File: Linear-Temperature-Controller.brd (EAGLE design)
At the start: 203.2 x 34.3 mm, 78 parts, among them IC1 LM393D, IC3 AD5624R, IC4 AD5262, IC5 LF356MX, T1 MMBT3904, T2 MMBT3904

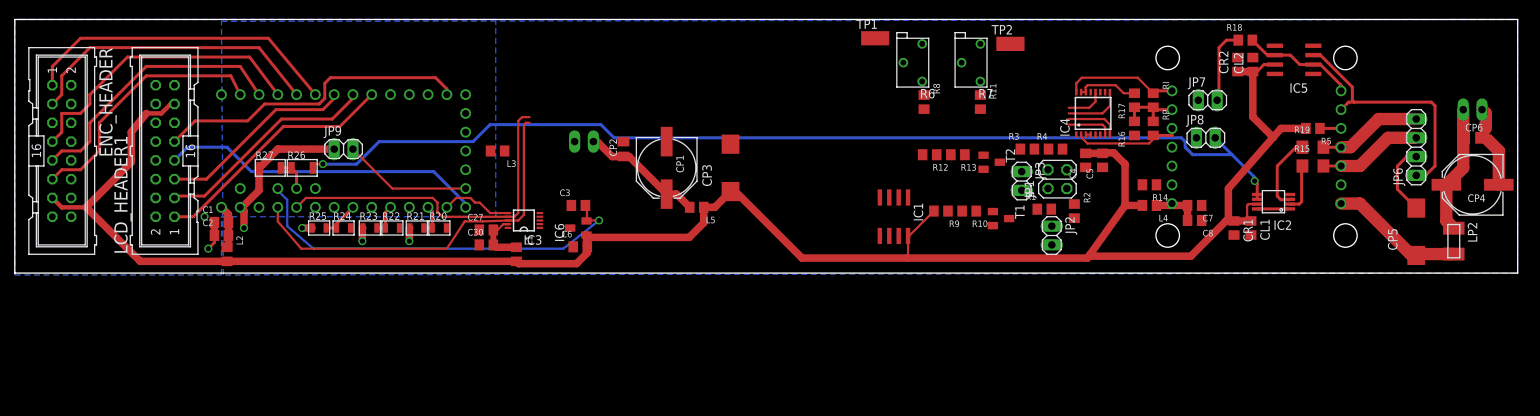
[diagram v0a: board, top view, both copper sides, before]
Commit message: Finished first attempt at board layout
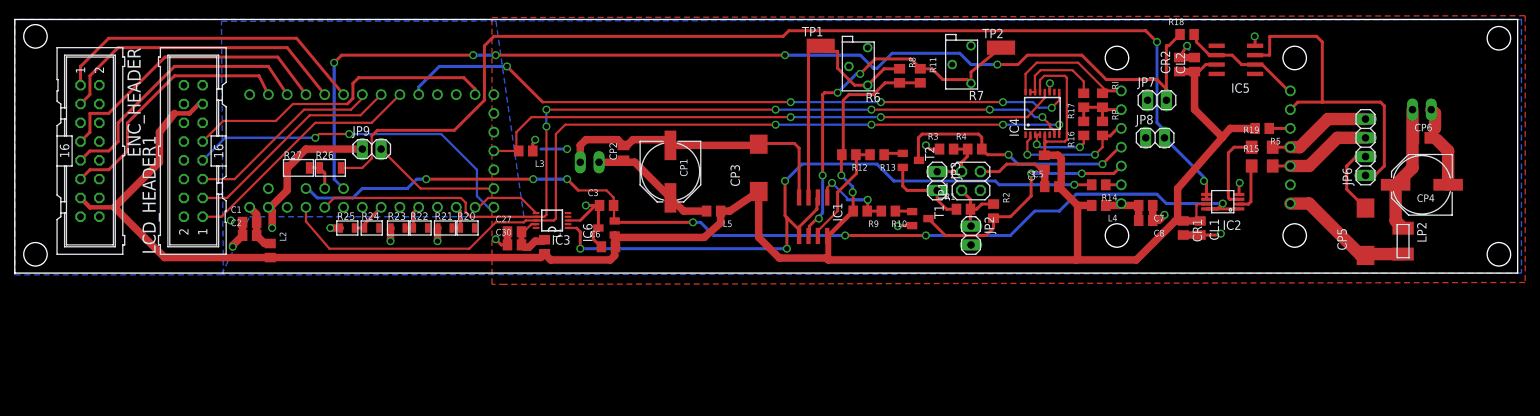
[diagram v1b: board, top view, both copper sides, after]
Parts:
- moved JP1 11.7 mm to (129.3, 12.4)
- moved JP3 11.4 mm to (124.7, 12.4)
- moved T2 10.9 mm to (121.2, 15.2)
- moved R10 10.9 mm to (118.1, 8.38)
- moved R3 10.9 mm to (126.0, 16.8)
- moved IC1 10.9 mm to (108.0, 7.62)
- moved JP2 10.9 mm to (129.3, 5.08)
- moved R1 10.9 mm to (128.3, 8.64)
- moved R12 10.9 mm to (112.8, 16.0)
- moved R13 10.9 mm to (116.6, 16.0)
- moved R2 10.9 mm to (132.3, 8.38)
- moved R4 10.9 mm to (129.8, 16.8)
- moved R9 10.9 mm to (114.3, 8.38)
- moved T1 10.9 mm to (122.4, 7.37)
- moved R11 8.87 mm to (122.4, 26.7)
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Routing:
- net ACT_T1: track 10.2 -> 146.5 mm, vias 0 -> 5
- net AGND: track 47.7 -> 157.2 mm, vias 4 -> 16
- net VSET1: track 0.00 -> 93.5 mm, vias 0 -> 4
- net CS_POT1: track 7.86 -> 92.6 mm, vias 0 -> 5
- net 2.5V: track 58.5 -> 140.2 mm, vias 1 -> 7
- net DGND: track 10.9 -> 84.1 mm, vias 2 -> 4
- net SCK_B: track 52.8 -> 117.1 mm, vias 0 -> 6
- net MOSI_B: track 59.5 -> 120.4 mm, vias 0 -> 4
- net N$7: track 0.00 -> 50.3 mm, vias 0 -> 4
- net VDD: track 267.0 -> 305.2 mm, vias 0 -> 2
- net N$6: track 0.00 -> 37.2 mm
- net N$3: track 0.00 -> 34.3 mm, vias 0 -> 2
- net N$1: track 0.00 -> 33.5 mm, vias 0 -> 2
- net N$8: track 0.00 -> 15.1 mm
- net N$9: track 0.00 -> 11.6 mm, vias 0 -> 2
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- added copper zone on layer 1, net AGND

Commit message: Clearance increased and added few vias
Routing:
- net ACT_T1: track 146.5 -> 140.4 mm, vias 5 -> 2
- net MON: track 17.4 -> 18.8 mm
- net SCK: track 47.0 -> 48.3 mm
- net AGND: vias 16 -> 59

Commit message: Fix minor errors on prototype schematic
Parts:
- added C10, C9: 0.1uF, rlc-jqi:0805
- R11: value 10k -> 33k
- R8: value 33k -> 10k
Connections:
- removed net 3.3V: U$1.3.3V, U$1.3.3V1
- new net N$21: LCD_HEADER1.13, U$1.3.3V, U$1.3.3V1
- net 2.5V: now also C10.2
- net AGND: now also C10.1, C9.1
- net N$23: no longer U1.P$8
- net N$6: now also IC1.2; no longer IC1.3
- net N$7: now also IC1.5; no longer IC1.6
- net VDD: now also IC4.10, IC4.6; no longer LCD_HEADER1.13
- net VMON1_B: now also C9.2
- net VSET1: now also IC1.3, IC1.6; no longer IC1.2, IC1.5
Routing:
- net N$6: track 37.2 -> 17.0 mm
- net VSET1: track 93.5 -> 92.5 mm
- net VDD: track 305.2 -> 304.7 mm
